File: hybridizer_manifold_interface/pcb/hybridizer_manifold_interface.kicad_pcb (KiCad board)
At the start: 2 copper layers, 85.6 x 132.2 mm, 79 parts, among them P1 HEADER_02X08_SMD, P2 HEADER_02X05_SMD, U1 HALL_DRV5053, U10 MAX4215, U11 HALL_DRV5053, U12 MAX4215, U13 HALL_DRV5053, U14 MAX4215, U2 MAX4215, U3 HALL_DRV5053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

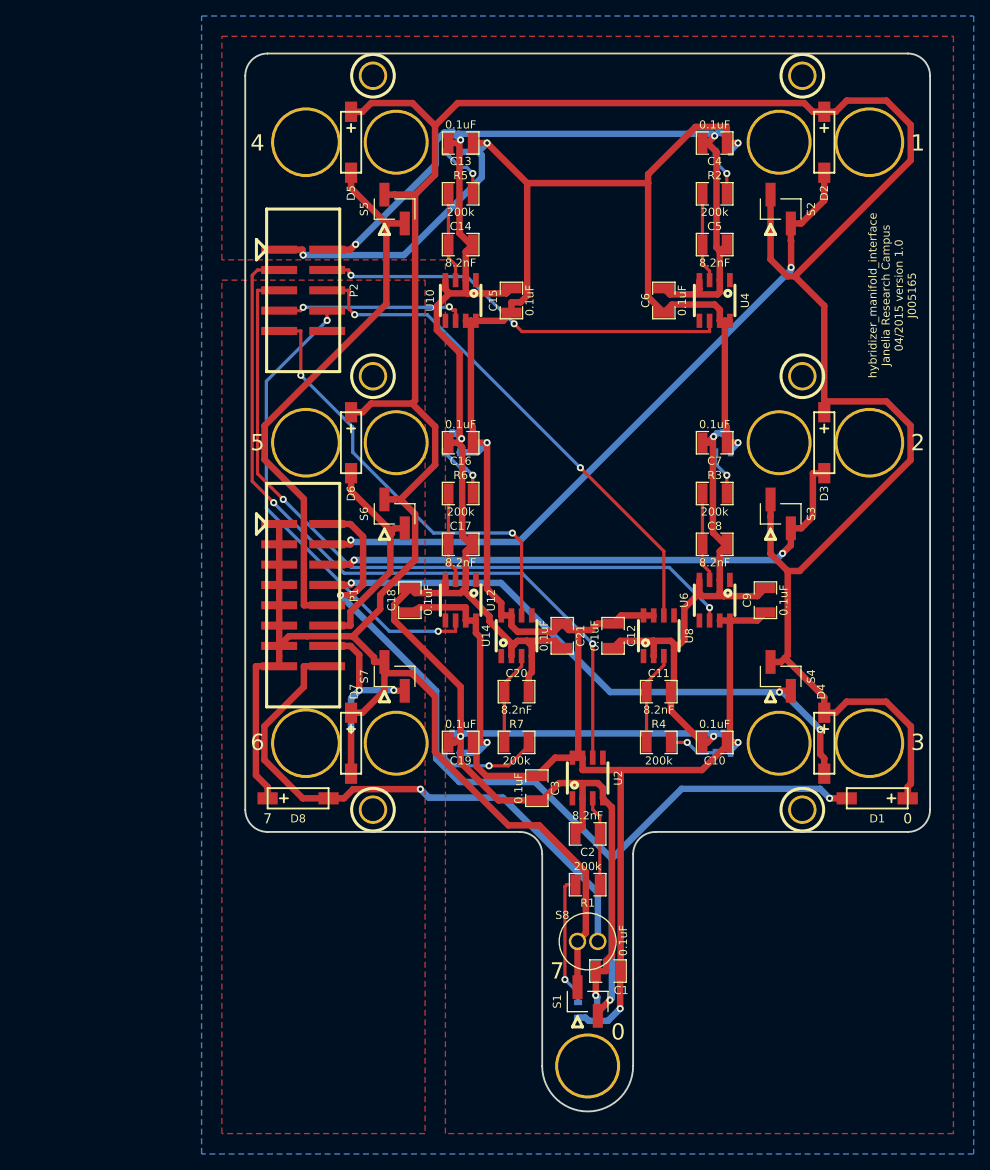
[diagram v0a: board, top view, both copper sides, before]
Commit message: Pcb design mostly finished.
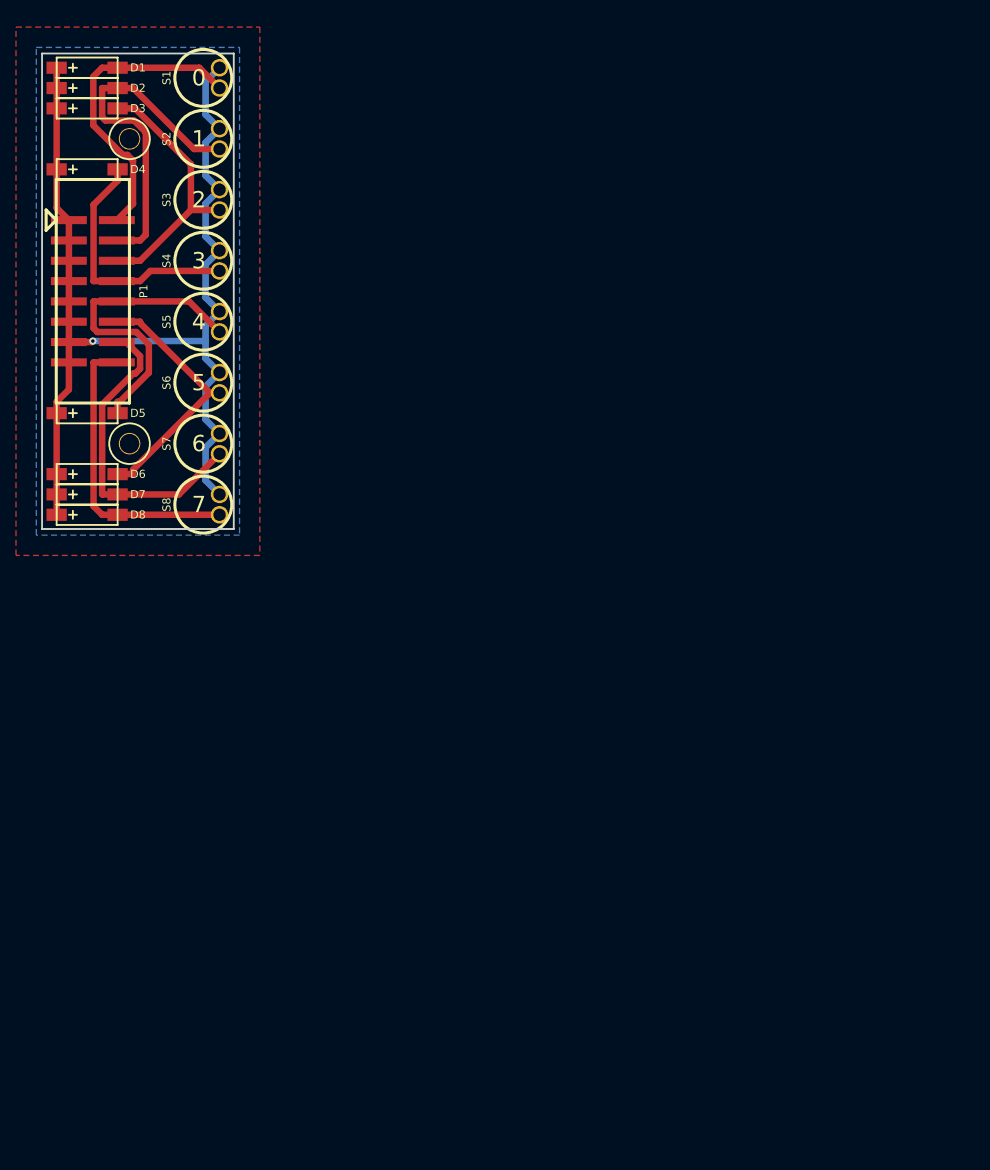
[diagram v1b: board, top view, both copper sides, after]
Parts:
- removed C1, C10, C12, C13, C15, C16, C18, C19, C21, C3, C4, C6, C7, C9: 0.1uF, hybridizer_manifold_interface:SM1210
- removed C11, C14, C17, C2, C20, C5, C8: 8.2nF, hybridizer_manifold_interface:SM1210
- removed CLEARANCE_HOLE_1, CLEARANCE_HOLE_2, CLEARANCE_HOLE_3, CLEARANCE_HOLE_4, CLEARANCE_HOLE_5, CLEARANCE_HOLE_6: clearance_hole, hybridizer_manifold_interface:clearance_hole
- removed MOUNTING_HOLE_2, MOUNTING_HOLE_3, MOUNTING_HOLE_4, MOUNTING_HOLE_5, MOUNTING_HOLE_6: mounting_hole, hybridizer_manifold_interface:mounting_hole
- removed P2: HEADER_02X05_SMD, hybridizer_manifold_interface:HEADER_02x05_SMD
- removed R1, R2, R3, R4, R5, R6, R7: 200k, hybridizer_manifold_interface:SM1210
- removed REF**, VALVE_HOLE_1, VALVE_HOLE_2, VALVE_HOLE_3, VALVE_HOLE_4, VALVE_HOLE_5, VALVE_HOLE_6: valve_hole, hybridizer_manifold_interface:valve_hole
- removed U1, U11, U13, U3, U5, U7, U9: HALL_DRV5053, hybridizer_manifold_interface:SOT-23-3
- removed U10, U12, U14, U2, U4, U6, U8: MAX4215, hybridizer_manifold_interface:SOIC_8_N
- added MOUNTING_HOLE_0: mounting_hole, hybridizer_manifold_interface:mounting_hole, F.Cu at (36.3, 36.1)
- S1, S2, S3, S4, S5, S6, S7: value HEADER_01X02_SMD -> LEE_VALVE_PLUG_IN; footprint hybridizer_manifold_interface:Header_2_Pin_SMD -> hybridizer_manifold_interface:LEE_VALVE_PLUG_IN
- moved D1 134.5 mm to (31.0, 27.2), turned to 90 degrees
- moved S1 124.3 mm to (47.6, 28.4), turned to 270 degrees
- moved D4 116.8 mm to (31.0, 39.9), turned to 90 degrees
- moved D3 101.2 mm to (31.0, 32.3), turned to 90 degrees
- moved MOUNTING_HOLE_1 95.9 mm to (36.3, 74.2)
- moved D2 92.4 mm to (31.0, 29.7), turned to 90 degrees
- moved S4 87.3 mm to (47.6, 51.3), turned to 270 degrees
- moved S3 80.4 mm to (47.6, 43.7), turned to 270 degrees
- moved S8 71.4 mm to (47.6, 81.8), turned to 270 degrees
- moved S2 70.7 mm to (47.6, 36.1), turned to 270 degrees
- moved D5 47.3 mm to (31.0, 70.4), turned to 90 degrees
- moved P1 46.2 mm to (31.8, 55.1)
- moved D7 45.3 mm to (31.0, 80.5), turned to 90 degrees
- moved D8 44.2 mm to (31.0, 83.1)
- moved S7 36.4 mm to (47.6, 74.2), turned to 270 degrees
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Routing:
- net GND: track 388.3 -> 0.00 mm, vias 8 -> 0
- net +5V: track 361.2 -> 0.00 mm, vias 8 -> 0
- net VAA: track 423.8 -> 137.8 mm, vias 0 -> 1
- net /A0: track 94.6 -> 0.00 mm, vias 2 -> 0
- net /A2: track 90.7 -> 0.00 mm, vias 2 -> 0
- net /OUT0: track 120.9 -> 38.5 mm, vias 3 -> 0
- net /A3: track 65.0 -> 0.00 mm, vias 2 -> 0
- net /A5: track 59.2 -> 0.00 mm, vias 2 -> 0
- net /A6: track 55.5 -> 0.00 mm, vias 2 -> 0
- net /A1: track 52.6 -> 0.00 mm, vias 2 -> 0
- net /OUT3: track 76.7 -> 31.5 mm, vias 3 -> 0
- net /OUT1: track 87.3 -> 44.4 mm, vias 2 -> 0
- net /OUT2: track 71.4 -> 33.2 mm, vias 2 -> 0
- net /OUT7: track 72.3 -> 37.1 mm, vias 1 -> 0
- net /OUT4: track 69.4 -> 38.8 mm
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- added copper zone on B.Cu, net VAA
- removed copper zone on F.Cu, net +5V
- removed copper zone on B.Cu, net GND
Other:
- board size 85.6 x 132.2 mm -> 24 x 59.4 mm
- board text added: "hybridizer_manifold_interface Janelia Research Campus 04/2015 version 1.0 J005166"
- board text removed: "hybridizer_manifold_interface Janelia Research Campus 04/2015 version 1.0 J005165"
